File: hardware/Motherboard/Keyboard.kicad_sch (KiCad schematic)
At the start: 0 parts

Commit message: WIP
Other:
- title: (none) -> Apollo 7 Squale 
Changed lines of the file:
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@@
 	(generator_version "9.0")
 	(paper "A3")
+	(title_block
+		(title "Apollo 7 Squale ")
+		(rev "0.1")
+		(comment 1 "http://hxc2001.free.fr/Squale/")
+		(comment 2 "CC-BY Licence (Creative Commons Attribution)")
+		(comment 3 "Drawn by Jean-François DEL NERO")
+	)
 )

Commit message: WIP -rom pack
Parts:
- added J11: Conn_01x22_Socket, symbol Connector:Conn_01x22_Socket
- added R49: 330R, symbol Device:R
- added U30: 74LS17, symbol 74xx:74LS07
- added U75: 6821, Package_DIP:DIP-40_W15.24mm, symbol Interface:6821
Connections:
- new net: R49.1, U30.8
- new net EB: U75.25 (ENABLE)
- new net KEYB_C1: J11.6 (Pin_6), U75.3 (PA1)
- new net KEYB_C2: J11.7 (Pin_7), U75.4 (PA2)
- new net KEYB_C3: J11.8 (Pin_8), U75.5 (PA3)
- new net KEYB_C4: J11.9 (Pin_9), U75.6 (PA4)
- new net KEYB_C5: J11.10 (Pin_10), U75.7 (PA5)
- new net KEYB_C6: J11.11 (Pin_11), U75.8 (PA6)
- new net KEYB_C7: J11.12 (Pin_12), U75.9 (PA7)
- new net KEYB_CTRL: J11.1 (Pin_1)
- new net KEYB_LED: J11.4 (Pin_4), R49.2
- new net KEYB_LOCK: J11.3 (Pin_3)
- new net KEYB_R0: J11.13 (Pin_13), U75.10 (PB0)
- new net KEYB_R1: J11.14 (Pin_14), U75.11 (PB1)
- new net KEYB_R2: J11.15 (Pin_15), U75.12 (PB2)
- new net KEYB_R3: J11.16 (Pin_16), U75.13 (PB3)
- new net KEYB_R4: J11.17 (Pin_17), U75.14 (PB4)
- new net KEYB_R5: J11.18 (Pin_18), U75.15 (PB5)
- new net KEYB_R6: J11.19 (Pin_19), U75.16 (PB6)
- new net KEYB_R7: J11.20 (Pin_20), U75.17 (PB7)
- new net KEYB_SHIFT: J11.2 (Pin_2)
- new net PA0: U75.36 (RS0)
- new net PA1: U75.35 (RS1)
- new net PA2: U75.24 (CS1)
- new net PD0: U75.33 (D0)
- new net PD1: U75.32 (D1)
- new net PD2: U75.31 (D2)
- new net PD3: U75.30 (D3)
- new net PD4: U75.29 (D4)
- new net PD5: U75.28 (D5)
- new net PD6: U75.27 (D6)
- new net PD7: U75.26 (D7)
- new net ROMPACK_RST_ADDR: U75.19 (CB2)
- new net R~{W}B: U75.21 (R/~{W})
- new net SYSREG_KEYB_LED: U30.9
- new net VCC5V: J11.22 (Pin_22), U75.20 (VCC), U75.22 (CS0)
- new net VSS: J11.5 (Pin_5), U75.1 (VSS)
- new net ~{CS_PIA}: U75.23 (~{CS2})
- new net ~{RSTB}: U75.34 (~{RESET})
- new net ~{RST}: J11.21 (Pin_21)
- no-connect marks 0 -> 6
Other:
- note added: "Base : 0xF044"

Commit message: S30 bus + annotations fixes.
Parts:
- renumbered U30 to U33
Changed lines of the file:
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@@
 		(dnp no)
 		(fields_autoplaced yes)
-		(property "Reference" "U30"
+		(property "Reference" "U33"
 			(at 213.36 87.63 0)
 			(effects
@@
 			(project "Squale"
 				(path "/9e981419-a202-4dd8-b7ec-e1bde8e7b185/28814265-8855-4aa8-bc56-9a1926cdf9bc"
-					(reference "U30")
+					(reference "U33")
 					(unit 4)
 				)

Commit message: wip : modem
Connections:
- net SYSREG_KEYB_LED renamed SYS_KEYB_LED
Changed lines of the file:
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@@
 		)
 	)
-	(hierarchical_label "SYSREG_KEYB_LED"
+	(hierarchical_label "SYS_KEYB_LED"
 		(shape input)
 		(at 63.5 96.52 180)

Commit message: WIP : passives parts, cosmetic stuffs.
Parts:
- added C69: 100nF, symbol Device:C
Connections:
- net VCC5V: now also C69.1
- net VSS: now also C69.2

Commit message: Footprints.
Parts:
- C69: footprint (none) -> Capacitor_THT:C_Disc_D9.0mm_W2.5mm_P5.00mm
- J11: footprint (none) -> Connector_PinHeader_2.54mm:PinHeader_1x22_P2.54mm_Vertical
- R49: footprint (none) -> Resistor_THT:R_Axial_DIN0309_L9.0mm_D3.2mm_P12.70mm_Horizontal
- U33: footprint (none) -> Package_DIP:DIP-14_W7.62mm_Socket
- U75: footprint Package_DIP:DIP-40_W15.24mm -> Package_DIP:DIP-40_W15.24mm_Socket
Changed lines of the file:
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@@
 			)
 		)
-		(property "Footprint" ""
+		(property "Footprint" "Package_DIP:DIP-14_W7.62mm_Socket"
 			(at 213.36 96.52 0)
 			(effects
@@
 			)
 		)
-		(property "Footprint" ""
+		(property "Footprint" "Resistor_THT:R_Axial_DIN0309_L9.0mm_D3.2mm_P12.70mm_Horizontal"
 			(at 229.87 98.298 90)
 			(effects
@@
 			)
 		)
-		(property "Footprint" ""
+		(property "Footprint" "Connector_PinHeader_2.54mm:PinHeader_1x22_P2.54mm_Vertical"
 			(at 276.86 128.27 0)
 			(effects
@@
 			)
 		)
-		(property "Footprint" "Package_DIP:DIP-40_W15.24mm"
+		(property "Footprint" "Package_DIP:DIP-40_W15.24mm_Socket"
 			(at 199.39 177.8 0)
 			(effects
@@
 			)
 		)
-		(property "Footprint" ""
+		(property "Footprint" "Capacitor_THT:C_Disc_D9.0mm_W2.5mm_P5.00mm"
 			(at 172.4152 190.5 0)
 			(effects

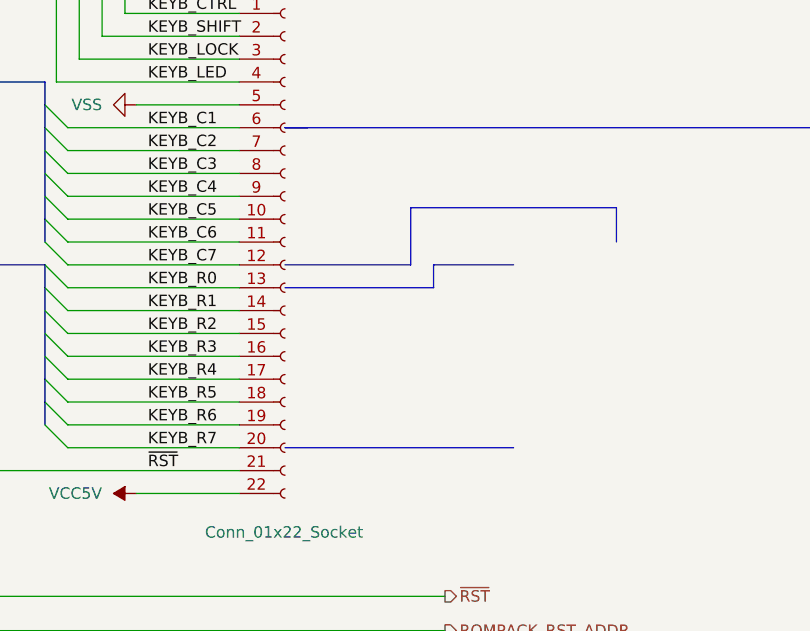
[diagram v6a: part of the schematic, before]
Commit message: add some descriptions / comments.
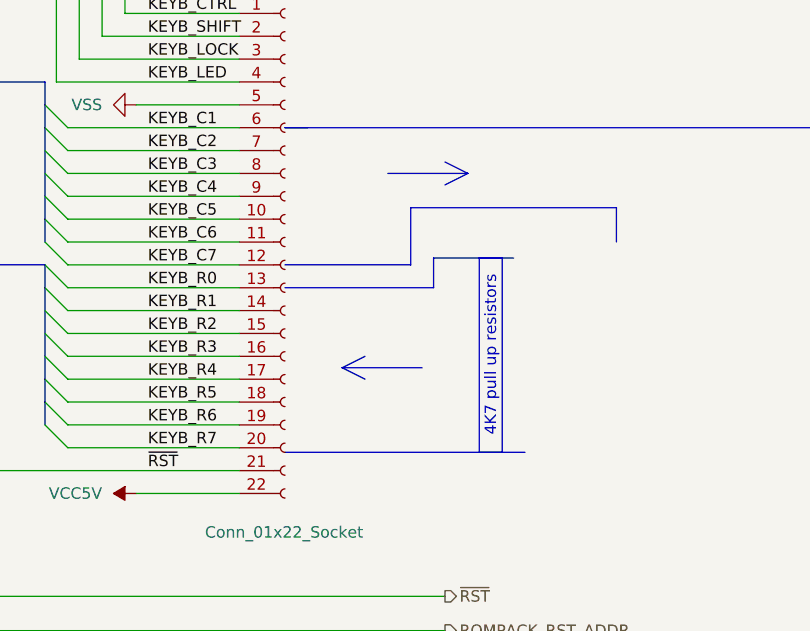
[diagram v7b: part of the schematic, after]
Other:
- note added: "4K7 pull up resistors"
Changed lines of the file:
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@@
 		(comment 3 "Drawn by Jean-François DEL NERO")
+	)
+	(rectangle
+		(start 298.45 130.048)
+		(end 300.99 151.638)
+		(stroke
+			(width 0)
+			(type default)
+		)
+		(fill
+			(type none)
+		)
+	)
+	(text "4K7 pull up resistors"
+		(exclude_from_sim no)
+		(at 299.72 140.97 90)
+		(effects
+			(font
+				(size 1.27 1.27)
+			)
+		)
 	)
 	(text "Base : 0xF044\n"
@@
 	(polyline
 		(pts
-			(xy 293.37 130.81) (xy 302.26 130.81)
+			(xy 293.37 130.048) (xy 302.26 130.048)
 		)
 		(stroke
@@
 		)
 	)
+	(polyline
+		(pts
+			(xy 297.18 120.65) (xy 288.29 120.65)
+		)
+		(stroke
+			(width 0)
+			(type default)
+		)
+	)
 	(wire
 		(pts
@@
 		)
 	)
+	(polyline
+		(pts
+			(xy 283.21 142.24) (xy 292.1 142.24)
+		)
+		(stroke
+			(width 0)
+			(type default)
+		)
+	)
 	(bus
 		(pts
@@
 		)
 	)
+	(polyline
+		(pts
+			(xy 283.21 142.24) (xy 285.75 143.51)
+		)
+		(stroke
+			(width 0)
+			(type default)
+		)
+	)
 	(bus
 		(pts
@@
 		)
 	)
+	(polyline
+		(pts
+			(xy 276.86 151.638) (xy 303.53 151.638)
+		)
+		(stroke
+			(width 0)
+			(type default)
+		)
+	)
 	(bus
 		(pts
@@
 	(polyline
 		(pts
-			(xy 276.86 151.13) (xy 302.26 151.13)
-		)
-		(stroke
-			(width 0)
-			(type default)
-		)
-	)
-	(polyline
-		(pts
 			(xy 384.81 115.57) (xy 384.81 127)
 		)
@@
 	(polyline
 		(pts
-			(xy 293.37 133.35) (xy 293.37 130.81)
+			(xy 293.37 133.35) (xy 293.37 130.048)
 		)
 		(stroke
@@
 		)
 	)
+	(polyline
+		(pts
+			(xy 297.18 120.65) (xy 294.64 121.92)
+		)
+		(stroke
+			(width 0)
+			(type default)
+		)
+	)
 	(bus
 		(pts
@@
 		)
 	)
+	(polyline
+		(pts
+			(xy 297.18 120.65) (xy 294.64 119.38)
+		)
+		(stroke
+			(width 0)
+			(type default)
+		)
+	)
 	(bus
 		(pts
@@
 		)
 		(stroke
+			(width 0)
+			(type default)
+		)
+	)
+	(polyline
+		(pts
+			(xy 283.21 142.24) (xy 285.75 140.97)
+		)
+		(stroke
